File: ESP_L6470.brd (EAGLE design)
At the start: 41.9 x 90.2 mm, 43 parts, among them IC2 CP2104, J1 MICRO-USB, J2 POWER_JACKPTH_LOCK, Q1 600mA/40V, Q2 600mA/40V, U1 L6470, U2 ESP-WROOM-03, U3 RGB-LED

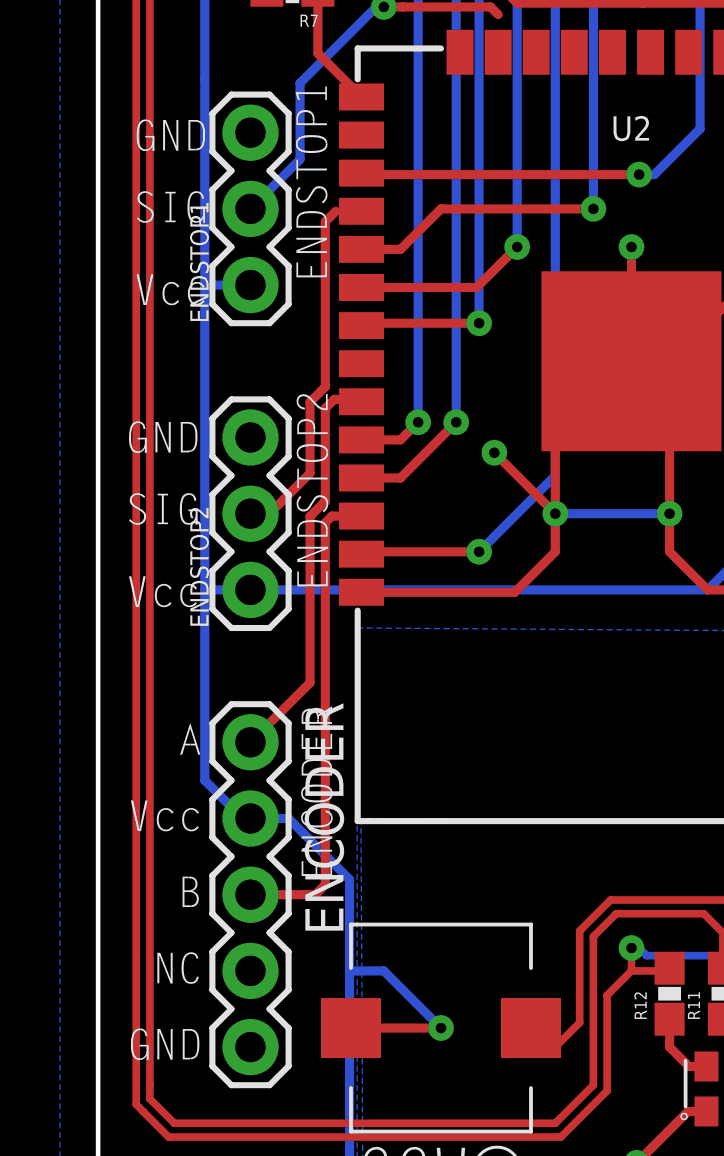
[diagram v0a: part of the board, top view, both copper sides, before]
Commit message: renamed some parts
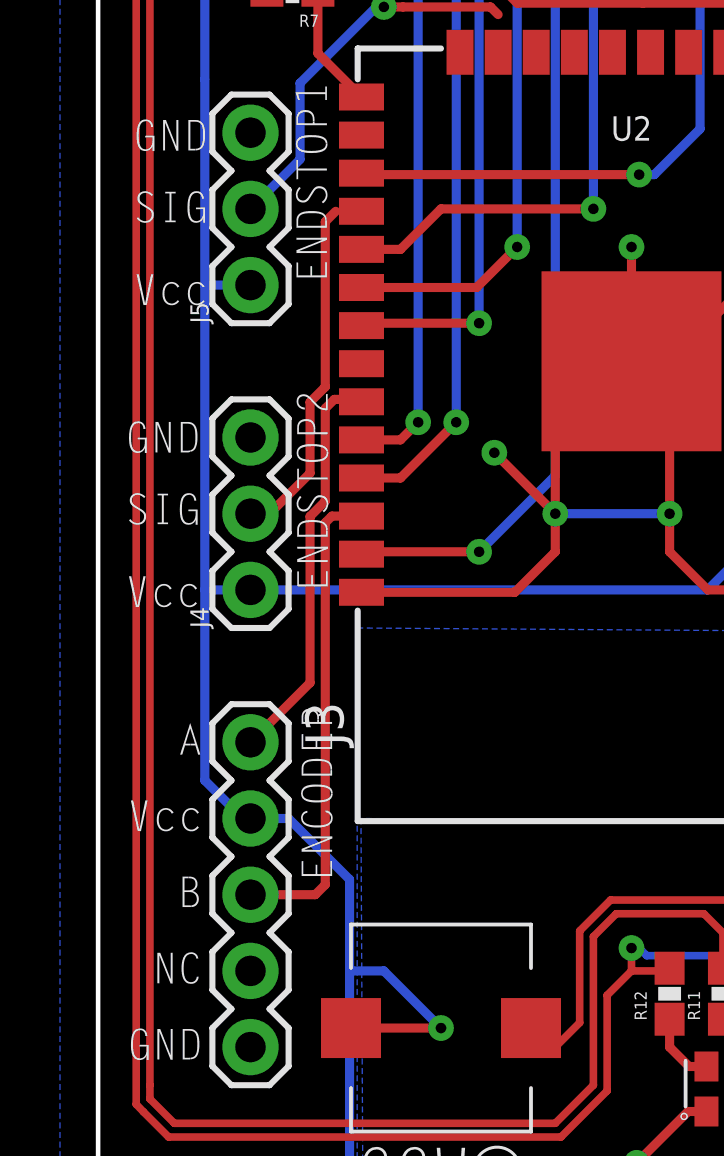
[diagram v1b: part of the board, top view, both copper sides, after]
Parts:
- J4: value ENDSTOP1 -> ENDSTOP2
- renumbered ENCODER to J3, ENDSTOP1 to J5, ENDSTOP2 to J4, U$18 to S1, U$19 to S2, U$23 to S4, U$24 to S3
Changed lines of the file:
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@@
 <element name="R9" library="SparkFun-Passives" package="0603-RES" value="12k" x="13.335" y="64.262" rot="R180"/>
 <element name="R10" library="SparkFun-Passives" package="0603-RES" value="12k" x="11.557" y="61.595"/>
-<element name="ENCODER" library="SparkFun-Connectors" package="1X05" value="ENCODER" x="6.35" y="29.21" rot="R270"/>
-<element name="ENDSTOP1" library="SparkFun-Connectors" package="1X03" value="ENDSTOP1" x="6.35" y="44.45" rot="R90"/>
-<element name="ENDSTOP2" library="SparkFun-Connectors" package="1X03" value="ENDSTOP1" x="6.35" y="34.29" rot="R90"/>
+<element name="J3" library="SparkFun-Connectors" package="1X05" value="ENCODER" x="6.35" y="29.21" rot="R270"/>
+<element name="J5" library="SparkFun-Connectors" package="1X03" value="ENDSTOP1" x="6.35" y="44.45" rot="R90"/>
+<element name="J4" library="SparkFun-Connectors" package="1X03" value="ENDSTOP2" x="6.35" y="34.29" rot="R90"/>
 <element name="U$5" library="IAD_ZHDK" package="TRACO12433" value="TRACO12433" x="15.24" y="85.09"/>
 <element name="STEPER" library="SparkFun-Connectors" package="1X04_LOCK_LONGPADS" value="STEPER" x="25.4" y="87.63">
@@
 <attribute name="SF_ID" value="PRT-00119" x="46.99" y="36.195" size="1.778" layer="27" rot="R90" display="off"/>
 </element>
-<element name="U$18" library="IAD-Library" package="B3AL-1002P-MS" value="B3AL-1002P-MS" x="12.7" y="10.16" rot="R180"/>
-<element name="U$19" library="IAD-Library" package="B3AL-1002P-MS" value="B3AL-1002P-MS" x="12.7" y="19.685" rot="R180"/>
-<element name="U$23" library="IAD-Library" package="B3AL-1002P-MS" value="B3AL-1002P-MS" x="22.225" y="10.16" rot="R180"/>
-<element name="U$24" library="IAD-Library" package="B3AL-1002P-MS" value="B3AL-1002P-MS" x="31.75" y="10.16" rot="R180"/>
+<element name="S1" library="IAD-Library" package="B3AL-1002P-MS" value="B3AL-1002P-MS" x="12.7" y="10.16" rot="R180"/>
+<element name="S2" library="IAD-Library" package="B3AL-1002P-MS" value="B3AL-1002P-MS" x="12.7" y="19.685" rot="R180"/>
+<element name="S4" library="IAD-Library" package="B3AL-1002P-MS" value="B3AL-1002P-MS" x="22.225" y="10.16" rot="R180"/>
+<element name="S3" library="IAD-Library" package="B3AL-1002P-MS" value="B3AL-1002P-MS" x="31.75" y="10.16" rot="R180"/>
 <element name="IC2" library="microbuilder" package="QFN24_4MM_SMSC" value="CP2104" x="7.112" y="71.247" smashed="yes" rot="R270"/>
 <element name="JP2" library="SparkFun-Jumpers" package="SMT-JUMPER_2_NC_TRACE_NO-SILK" value="JUMPER-SMT_2_NC_TRACE_NO-SILK" x="12.065" y="67.31" rot="R270"/>
@@
 <contactref element="U2" pad="15"/>
 <contactref element="U2" pad="1"/>
-<contactref element="ENCODER" pad="5"/>
+<contactref element="J3" pad="5"/>
 <wire x1="31.874" y1="78.232" x2="32.131" y2="78.489" width="0.254" layer="1"/>
 <polygon width="0.254" layer="16" isolate="0.3048" rank="3">
@@
 <wire x1="22.01" y1="59.69" x2="20.32" y2="59.69" width="0.254" layer="1"/>
 <via x="20.32" y="59.69" extent="1-16" drill="0.508"/>
-<contactref element="ENDSTOP2" pad="3"/>
-<contactref element="ENDSTOP1" pad="3"/>
+<contactref element="J4" pad="3"/>
+<contactref element="J5" pad="3"/>
 <contactref element="U$5" pad="GND"/>
 <wire x1="28.05" y1="34.21" x2="27.97" y2="34.29" width="0.3048" layer="1"/>
@@
 <contactref element="R8" pad="2"/>
 <contactref element="R7" pad="2"/>
-<contactref element="ENCODER" pad="2"/>
+<contactref element="J3" pad="2"/>
 <contactref element="U1" pad="17"/>
 <contactref element="R1" pad="2"/>
@@
 <wire x1="32.131" y1="75.689" x2="30.184" y2="75.689" width="0.3048" layer="1"/>
 <wire x1="30.184" y1="75.689" x2="29.972" y2="75.477" width="0.254" layer="1"/>
-<contactref element="ENDSTOP1" pad="1"/>
-<contactref element="ENDSTOP2" pad="1"/>
+<contactref element="J5" pad="1"/>
+<contactref element="J4" pad="1"/>
 <wire x1="27.94" y1="77.685" x2="28.741" y2="77.685" width="0.3048" layer="1"/>
 <wire x1="28.741" y1="77.685" x2="28.829" y2="77.597" width="0.3048" layer="1"/>
@@
 <wire x1="4.826" y1="51.308" x2="4.826" y2="44.45" width="0.3048" layer="16"/>
 <wire x1="4.826" y1="51.308" x2="4.826" y2="55.88" width="0.3048" layer="16"/>
-<contactref element="U$18" pad="P$2"/>
-<contactref element="U$19" pad="P$2"/>
-<contactref element="U$24" pad="P$2"/>
-<contactref element="U$23" pad="P$2"/>
+<contactref element="S1" pad="P$2"/>
+<contactref element="S2" pad="P$2"/>
+<contactref element="S3" pad="P$2"/>
+<contactref element="S4" pad="P$2"/>
 <wire x1="4.826" y1="55.88" x2="4.826" y2="57.15" width="0.3048" layer="16"/>
 <wire x1="4.826" y1="57.15" x2="4.826" y2="60.96" width="0.3048" layer="16"/>
@@
 </signal>
 <signal name="ENDSTOP1">
-<contactref element="ENDSTOP1" pad="2"/>
+<contactref element="J5" pad="2"/>
 <wire x1="14.605" y1="53.467" x2="14.351" y2="53.721" width="0.3048" layer="1"/>
 <wire x1="14.351" y1="53.721" x2="11.43" y2="53.721" width="0.3048" layer="1"/>
@@
 </signal>
 <signal name="ENDSTOP2">
-<contactref element="ENDSTOP2" pad="2"/>
+<contactref element="J4" pad="2"/>
 <wire x1="6.43" y1="36.75" x2="6.35" y2="36.83" width="0.3048" layer="1"/>
 <wire x1="6.35" y1="36.83" x2="6.985" y2="36.83" width="0.3048" layer="1"/>
@@
 </signal>
 <signal name="ENC_A">
-<contactref element="ENCODER" pad="1"/>
+<contactref element="J3" pad="1"/>
 <contactref element="U2" pad="33"/>
 <wire x1="6.35" y1="29.21" x2="8.3348" y2="31.1948" width="0.3048" layer="1"/>
@@
 </signal>
 <signal name="ENC_B">
-<contactref element="ENCODER" pad="3"/>
+<contactref element="J3" pad="3"/>
 <contactref element="U2" pad="36"/>
 <wire x1="10.05" y1="36.75" x2="9.064" y2="36.75" width="0.3048" layer="1"/>
@@
 </signal>
 <signal name="NC">
-<contactref element="ENCODER" pad="4"/>
+<contactref element="J3" pad="4"/>
 </signal>
 <signal name="N$8">
@@
 <signal name="DOWN">
 <contactref element="U2" pad="11"/>
-<contactref element="U$18" pad="P$1"/>
+<contactref element="S1" pad="P$1"/>
 <wire x1="28.05" y1="46.91" x2="28.13" y2="46.99" width="0.3048" layer="1"/>
 <wire x1="28.05" y1="46.91" x2="29.163" y2="46.91" width="0.254" layer="1"/>
@@
 </signal>
 <signal name="UP">
-<contactref element="U$19" pad="P$1"/>
+<contactref element="S2" pad="P$1"/>
 <contactref element="U2" pad="9"/>
 <wire x1="28.05" y1="44.37" x2="28.13" y2="44.45" width="0.3048" layer="1"/>
@@
 </signal>
 <signal name="STOP">
-<contactref element="U$24" pad="P$1"/>
+<contactref element="S3" pad="P$1"/>
 <contactref element="U2" pad="14"/>
 <wire x1="28.05" y1="50.72" x2="28.13" y2="50.8" width="0.3048" layer="1"/>
@@
 </signal>
 <signal name="HOME">
-<contactref element="U$23" pad="P$1"/>
+<contactref element="S4" pad="P$1"/>
 <contactref element="U2" pad="12"/>
 <wire x1="28.05" y1="48.18" x2="28.4382" y2="47.7918" width="0.254" layer="1"/>

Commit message: renamed some parts
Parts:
- renumbered STEPER to J6, U$5 to U4
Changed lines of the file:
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@@
 <element name="R9" library="SparkFun-Passives" package="0603-RES" value="12k" x="13.335" y="64.262" rot="R180"/>
 <element name="R10" library="SparkFun-Passives" package="0603-RES" value="12k" x="11.557" y="61.595"/>
-<element name="J3" library="SparkFun-Connectors" package="1X05" value="ENCODER" x="6.35" y="29.21" rot="R270"/>
-<element name="J5" library="SparkFun-Connectors" package="1X03" value="ENDSTOP1" x="6.35" y="44.45" rot="R90"/>
-<element name="J4" library="SparkFun-Connectors" package="1X03" value="ENDSTOP2" x="6.35" y="34.29" rot="R90"/>
-<element name="U$5" library="IAD_ZHDK" package="TRACO12433" value="TRACO12433" x="15.24" y="85.09"/>
-<element name="STEPER" library="SparkFun-Connectors" package="1X04_LOCK_LONGPADS" value="STEPER" x="25.4" y="87.63">
+<element name="J3" library="SparkFun-Connectors" package="1X05" value="ENCODER" x="6.35" y="29.21" smashed="yes" rot="R270">
+<attribute name="NAME" x="8.1788" y="30.5562" size="1.27" layer="25" ratio="10" rot="R270"/>
+</element>
+<element name="J5" library="SparkFun-Connectors" package="1X03" value="ENDSTOP1" x="6.35" y="44.45" smashed="yes" rot="R90">
+<attribute name="NAME" x="4.953" y="43.18" size="0.6096" layer="25" font="vector" ratio="20" rot="R90"/>
+</element>
+<element name="J4" library="SparkFun-Connectors" package="1X03" value="ENDSTOP2" x="6.35" y="34.29" smashed="yes" rot="R90">
+<attribute name="NAME" x="4.953" y="33.02" size="0.6096" layer="25" font="vector" ratio="20" rot="R90"/>
+</element>
+<element name="U4" library="IAD_ZHDK" package="TRACO12433" value="TRACO12433" x="15.24" y="85.09"/>
+<element name="J6" library="SparkFun-Connectors" package="1X04_LOCK_LONGPADS" value="STEPER" x="25.4" y="87.63" smashed="yes">
+<attribute name="NAME" x="24.13" y="89.408" size="1.27" layer="25" font="vector"/>
 <attribute name="PROD_ID" value="CONN-09696" x="25.4" y="87.63" size="1.778" layer="27" display="off"/>
 </element>
@@
 <contactref element="J4" pad="3"/>
 <contactref element="J5" pad="3"/>
-<contactref element="U$5" pad="GND"/>
+<contactref element="U4" pad="GND"/>
 <wire x1="28.05" y1="34.21" x2="27.97" y2="34.29" width="0.3048" layer="1"/>
 <wire x1="27.97" y1="34.29" x2="21.59" y2="34.29" width="0.3048" layer="1"/>
@@
 <wire x1="21.971" y1="63.119" x2="19.05" y2="66.04" width="0.8128" layer="1"/>
 <wire x1="19.05" y1="66.04" x2="19.05" y2="72.39" width="0.8128" layer="1"/>
-<contactref element="STEPER" pad="1"/>
+<contactref element="J6" pad="1"/>
 <wire x1="19.05" y1="72.39" x2="19.05" y2="80.772" width="0.8128" layer="1"/>
 <wire x1="25.4" y1="87.63" x2="19.05" y2="81.28" width="0.8128" layer="1"/>
@@
 <signal name="OUT2A">
 <contactref element="U1" pad="28"/>
-<contactref element="STEPER" pad="2"/>
+<contactref element="J6" pad="2"/>
 <wire x1="27.94" y1="87.376" x2="27.94" y2="86.36" width="1.27" layer="1"/>
 <wire x1="27.94" y1="86.36" x2="21.59" y2="80.01" width="0.8128" layer="1"/>
@@
 <wire x1="39.37" y1="82.55" x2="39.37" y2="64.77" width="0.8128" layer="1"/>
 <wire x1="39.37" y1="64.77" x2="37.719" y2="63.119" width="0.8128" layer="1"/>
-<contactref element="STEPER" pad="3"/>
+<contactref element="J6" pad="3"/>
 <wire x1="30.48" y1="87.63" x2="30.48" y2="90.17" width="0.8128" layer="1"/>
 <wire x1="30.48" y1="90.17" x2="31.75" y2="91.44" width="0.8128" layer="1"/>
@@
 <signal name="OUT2B">
 <contactref element="U1" pad="15"/>
-<contactref element="STEPER" pad="4"/>
+<contactref element="J6" pad="4"/>
 <wire x1="33.02" y1="87.376" x2="33.02" y2="83.82" width="0.8128" layer="1"/>
 <wire x1="33.02" y1="83.82" x2="36.83" y2="80.01" width="0.8128" layer="1"/>
@@
 <wire x1="28.829" y1="75.819" x2="29.171" y2="75.477" width="0.3048" layer="1"/>
 <wire x1="26.67" y1="59.69" x2="26.67" y2="57.15" width="0.3048" layer="1"/>
-<contactref element="U$5" pad="3.3VOUT"/>
+<contactref element="U4" pad="3.3VOUT"/>
 <wire x1="15.24" y1="82.55" x2="17.78" y2="80.01" width="0.3048" layer="1"/>
 <via x="17.78" y="77.724" extent="1-16" drill="0.35"/>
@@
 <wire x1="26.289" y1="68.453" x2="26.289" y2="69.006" width="0.254" layer="1"/>
 <wire x1="26.289" y1="69.006" x2="26.285" y2="69.01" width="0.254" layer="1"/>
-<contactref element="U$5" pad="VIN"/>
+<contactref element="U4" pad="VIN"/>
 <wire x1="36.068" y1="58.205" x2="34.755" y2="58.205" width="0.3048" layer="1"/>
 <wire x1="34.755" y1="58.205" x2="34.655" y2="58.105" width="0.3048" layer="1"/>

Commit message: renamed aesthetics
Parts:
- renumbered U$13 to A2, U$15 to A1
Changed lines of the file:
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@@
 <element name="U$11" library="RP400N501A" package="STAND-OFF" value="" x="40.64" y="90.17"/>
 <element name="U$12" library="RP400N501A" package="STAND-OFF" value="" x="3.81" y="90.17"/>
-<element name="U$13" library="IAD_GRAPHIC" package="INTERFACE_NETSTEPPER" value="INTERFACE_NETSTEPPER" x="3.81" y="5.08"/>
-<element name="U$15" library="IAD_GRAPHIC" package="ZHDK_LOGO" value="ZHDK_LOGO_METAL" x="8.89" y="81.28" rot="R90"/>
+<element name="A2" library="IAD_GRAPHIC" package="INTERFACE_NETSTEPPER" value="INTERFACE_NETSTEPPER" x="3.81" y="5.08"/>
+<element name="A1" library="IAD_GRAPHIC" package="ZHDK_LOGO" value="ZHDK_LOGO_METAL" x="8.89" y="81.28" rot="R90"/>
 </elements>
 <signals>

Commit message: fixed tx and rx pins and removed jumpers
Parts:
- removed JP2, JP3: JUMPER-SMT_2_NC_TRACE_NO-SILK, SparkFun-Jumpers:SMT-JUMPER_2_NC_TRACE_NO-SILK
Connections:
- removed net RXD0: IC2.21, JP2.1
- removed net TXD0: IC2.20, JP3.1
- net RX: now also IC2.21; no longer JP3.2
- net TX: now also IC2.20; no longer JP2.2
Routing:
- net RX: track 29.8 -> 36.6 mm
- net TX: track 31.2 -> 36.9 mm
- net RXD0: track 5.31 -> 0.00 mm
- net TXD0: track 3.88 -> 0.00 mm
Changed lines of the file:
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@@
 <drawing>
 <settings>
-<setting alwaysvectorfont="yes"/>
+<setting alwaysvectorfont="no"/>
 <setting keepoldvectorfont="yes"/>
 <setting verticaltext="up"/>
@@
 <element name="S3" library="IAD-Library" package="B3AL-1002P-MS" value="B3AL-1002P-MS" x="31.75" y="10.16" rot="R180"/>
 <element name="IC2" library="microbuilder" package="QFN24_4MM_SMSC" value="CP2104" x="7.112" y="71.247" smashed="yes" rot="R270"/>
-<element name="JP2" library="SparkFun-Jumpers" package="SMT-JUMPER_2_NC_TRACE_NO-SILK" value="JUMPER-SMT_2_NC_TRACE_NO-SILK" x="12.065" y="67.31" rot="R270"/>
-<element name="JP3" library="SparkFun-Jumpers" package="SMT-JUMPER_2_NC_TRACE_NO-SILK" value="JUMPER-SMT_2_NC_TRACE_NO-SILK" x="10.541" y="67.31" rot="R270"/>
 <element name="J1" library="SparkFun-Connectors" package="USB-MICROB" value="MICRO-USB" x="2.667" y="80.137" rot="R180">
 <attribute name="PROD_ID" value="CONN-09505" x="10.287" y="76.327" size="1.778" layer="27" rot="R180" display="off"/>
@@
 <signal name="TX">
 <contactref element="U2" pad="35"/>
-<contactref element="JP2" pad="2"/>
 <wire x1="10.05" y1="38.02" x2="11.35" y2="38.02" width="0.3048" layer="1"/>
 <wire x1="11.35" y1="38.02" x2="13.208" y2="39.878" width="0.3048" layer="1"/>
@@
 <wire x1="13.208" y1="39.878" x2="13.208" y2="65.278" width="0.3048" layer="16"/>
 <wire x1="13.208" y1="65.278" x2="12.7" y2="66.04" width="0.3048" layer="16"/>
-<wire x1="12.7" y1="66.04" x2="12.7" y2="66.0428" width="0.3048" layer="16"/>
-<via x="12.7" y="66.0428" extent="1-16" drill="0.35"/>
-<wire x1="12.2174" y1="66.6021" x2="12.2174" y2="66.802" width="0.3048" layer="1"/>
-<wire x1="12.7" y1="66.0428" x2="12.7" y2="66.1195" width="0.3048" layer="1"/>
-<wire x1="12.7" y1="66.1195" x2="12.2174" y2="66.6021" width="0.3048" layer="1"/>
-<wire x1="12.2174" y1="66.802" x2="12.065" y2="66.802" width="0" layer="19" extent="1-1"/>
+<contactref element="IC2" pad="20"/>
+<wire x1="9.112" y1="70.497" x2="9.124" y2="70.485" width="0.3048" layer="1"/>
+<wire x1="9.124" y1="70.485" x2="10.287" y2="70.485" width="0.3048" layer="1"/>
+<wire x1="10.287" y1="70.485" x2="10.287" y2="69.342" width="0.3048" layer="1"/>
+<wire x1="10.287" y1="69.342" x2="10.541" y2="69.088" width="0.3048" layer="1"/>
+<via x="10.541" y="69.088" extent="1-16" drill="0.35"/>
+<wire x1="10.541" y1="69.088" x2="12.7" y2="66.929" width="0.3048" layer="16"/>
+<wire x1="12.7" y1="66.929" x2="12.7" y2="66.04" width="0.3048" layer="16"/>
 </signal>
 <signal name="RX">
 <contactref element="U2" pad="34"/>
-<contactref element="JP3" pad="2"/>
 <wire x1="10.05" y1="39.29" x2="11.35" y2="39.29" width="0.3048" layer="1"/>
 <via x="11.938" y="39.878" extent="1-16" drill="0.35"/>
@@
 <wire x1="10.541" y1="66.1195" x2="10.0584" y2="66.6021" width="0.3048" layer="1"/>
 <wire x1="11.938" y1="64.262" x2="10.541" y2="65.659" width="0.3048" layer="16"/>
-<wire x1="10.0584" y1="66.802" x2="10.541" y2="66.802" width="0" layer="19" extent="1-1"/>
+<contactref element="IC2" pad="21"/>
+<wire x1="10.0584" y1="66.802" x2="11.557" y2="68.3006" width="0.3048" layer="1"/>
+<wire x1="11.557" y1="68.3006" x2="11.557" y2="70.104" width="0.3048" layer="1"/>
+<wire x1="11.557" y1="70.104" x2="10.668" y2="70.993" width="0.3048" layer="1"/>
+<wire x1="9.761575" y1="70.993" x2="9.757575" y2="70.997" width="0.3048" layer="1"/>
+<wire x1="10.668" y1="70.993" x2="9.761575" y2="70.993" width="0.3048" layer="1"/>
+<wire x1="9.112" y1="70.997" x2="9.116" y2="70.993" width="0.3048" layer="1"/>
+<wire x1="9.116" y1="70.993" x2="9.761575" y2="70.993" width="0.3048" layer="1"/>
 </signal>
 <signal name="ENDSTOP1">
@@
 <wire x1="3.695" y1="71.997" x2="2.54" y2="73.152" width="0.254" layer="1"/>
 </signal>
-<signal name="RXD0">
-<contactref element="IC2" pad="21"/>
-<contactref element="JP2" pad="1"/>
-<wire x1="9.112" y1="70.997" x2="10.664" y2="70.997" width="0.254" layer="1"/>
-<wire x1="12.065" y1="69.596" x2="10.664" y2="70.997" width="0.254" layer="1"/>
-<wire x1="12.065" y1="67.818" x2="12.065" y2="69.596" width="0.254" layer="1"/>
-</signal>
-<signal name="TXD0">
-<contactref element="IC2" pad="20"/>
-<contactref element="JP3" pad="1"/>
-<wire x1="9.112" y1="70.497" x2="10.148" y2="70.497" width="0.254" layer="1"/>
-<wire x1="10.148" y1="70.497" x2="10.287" y2="70.358" width="0.254" layer="1"/>
-<wire x1="10.287" y1="70.358" x2="10.287" y2="68.072" width="0.254" layer="1"/>
-<wire x1="10.287" y1="68.072" x2="10.541" y2="67.818" width="0.254" layer="1"/>
-</signal>
 <signal name="N$13">
